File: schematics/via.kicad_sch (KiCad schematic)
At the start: 8 parts, among them J6 Port A, J7 Port B, J8 myBus, Q1 2SB817, U6 W65C22, U7 74HC238

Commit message: Fix errors in schematics
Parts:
- renumbered J6 to J4, J7 to J5, J8 to J6
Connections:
- no-connect marks 19 -> 25
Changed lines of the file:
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@@
 	)
 	(no_connect
+		(at 168.91 134.62)
+	)
+	(no_connect
 		(at 153.67 134.62)
 	)
@@
 	)
 	(no_connect
+		(at 163.83 134.62)
+	)
+	(no_connect
+		(at 173.99 134.62)
+	)
+	(no_connect
 		(at 182.88 66.04)
 	)
 	(no_connect
+		(at 166.37 134.62)
+	)
+	(no_connect
 		(at 182.88 71.12)
 	)
@@
 	)
 	(no_connect
+		(at 171.45 134.62)
+	)
+	(no_connect
 		(at 151.13 134.62)
 	)
 	(no_connect
+		(at 161.29 134.62)
+	)
+	(no_connect
 		(at 182.88 81.28)
 	)
@@
 		)
 	)
+	(label "D[0..7]"
+		(at 118.11 118.11 90)
+		(fields_autoplaced yes)
+		(effects
+			(font
+				(size 1.27 1.27)
+				(bold yes)
+			)
+			(justify left bottom)
+		)
+	)
 	(label "PA4"
 		(at 100.33 62.23 0)
@@
 		)
 	)
+	(label "PA[0..7]"
+		(at 82.55 67.31 0)
+		(fields_autoplaced yes)
+		(effects
+			(font
+				(size 1.27 1.27)
+				(bold yes)
+			)
+			(justify left bottom)
+		)
+	)
 	(label "D2"
 		(at 135.89 125.73 90)
@@
 		)
 	)
+	(label "PB[0..7]"
+		(at 82.55 105.41 0)
+		(fields_autoplaced yes)
+		(effects
+			(font
+				(size 1.27 1.27)
+				(thickness 0.254)
+				(bold yes)
+			)
+			(justify left bottom)
+		)
+	)
 	(label "A2"
 		(at 115.57 132.08 90)
@@
 		)
 	)
+	(label "A[0..3]"
+		(at 109.22 120.65 90)
+		(fields_autoplaced yes)
+		(effects
+			(font
+				(size 1.27 1.27)
+				(bold yes)
+			)
+			(justify left bottom)
+		)
+	)
 	(label "PB2"
 		(at 50.8 93.98 0)
@@
 		(dnp no)
 		(fields_autoplaced yes)
-		(property "Reference" "J7"
+		(property "Reference" "J5"
 			(at 62.865 73.66 0)
 			(effects
@@
 			(project ""
 				(path "/03a78ca6-eaff-4f05-be7b-36cd15f8b56d/61a342ed-3f86-4ceb-b427-f3e043df7103"
-					(reference "J7")
+					(reference "J5")
 					(unit 1)
 				)
@@
 		(dnp no)
 		(fields_autoplaced yes)
-		(property "Reference" "J8"
+		(property "Reference" "J6"
 			(at 125.095 149.86 0)
 			(effects
@@
 			(project ""
 				(path "/03a78ca6-eaff-4f05-be7b-36cd15f8b56d/61a342ed-3f86-4ceb-b427-f3e043df7103"
-					(reference "J8")
+					(reference "J6")
 					(unit 1)
 				)
@@
 		(dnp no)
 		(fields_autoplaced yes)
-		(property "Reference" "J6"
+		(property "Reference" "J4"
 			(at 62.865 38.1 0)
 			(effects
@@
 			(project ""
 				(path "/03a78ca6-eaff-4f05-be7b-36cd15f8b56d/61a342ed-3f86-4ceb-b427-f3e043df7103"
-					(reference "J6")
+					(reference "J4")
 					(unit 1)
 				)

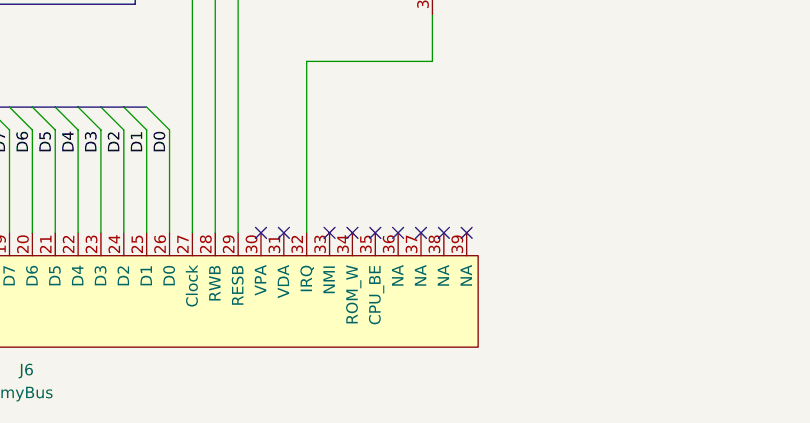
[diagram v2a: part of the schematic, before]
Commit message: Update ROM design
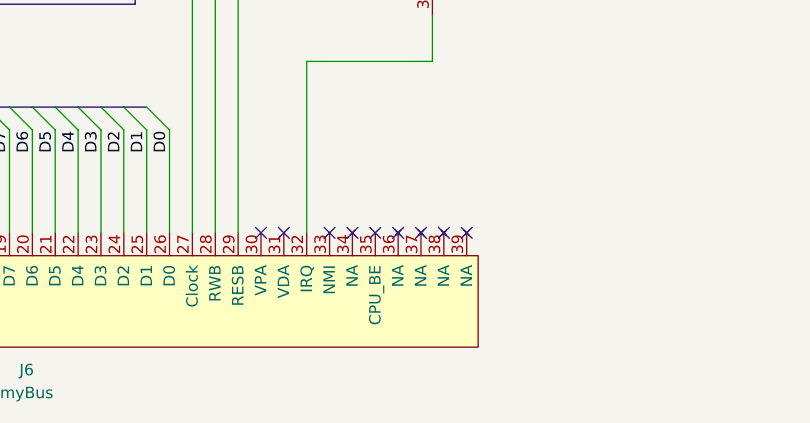
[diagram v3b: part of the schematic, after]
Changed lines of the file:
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@@
 	(label "D0"
 		(at 129.54 67.31 0)
-		(fields_autoplaced yes)
 		(effects
 			(font
@@
 	(label "CA1"
 		(at 128.27 49.53 0)
-		(fields_autoplaced yes)
 		(effects
 			(font
@@
 	(label "D1"
 		(at 138.43 125.73 90)
-		(fields_autoplaced yes)
 		(effects
 			(font
@@
 	(label "D6"
 		(at 125.73 125.73 90)
-		(fields_autoplaced yes)
 		(effects
 			(font
@@
 	(label "D[0..7]"
 		(at 118.11 118.11 90)
-		(fields_autoplaced yes)
 		(effects
 			(font
@@
 	(label "PA4"
 		(at 100.33 62.23 0)
-		(fields_autoplaced yes)
 		(effects
 			(font
@@
 	(label "PB6"
 		(at 100.33 87.63 0)
-		(fields_autoplaced yes)
 		(effects
 			(font
@@
 	(label "D6"
 		(at 129.54 82.55 0)
-		(fields_autoplaced yes)
 		(effects
 			(font
@@
 	(label "PA[0..7]"
 		(at 82.55 67.31 0)
-		(fields_autoplaced yes)
 		(effects
 			(font
@@
 	(label "D2"
 		(at 135.89 125.73 90)
-		(fields_autoplaced yes)
 		(effects
 			(font
@@
 	(label "CB2"
 		(at 105.41 95.25 180)
-		(fields_autoplaced yes)
 		(effects
 			(font
@@
 	(label "CA2"
 		(at 128.27 52.07 0)
-		(fields_autoplaced yes)
 		(effects
 			(font
@@
 	(label "PB[0..7]"
 		(at 82.55 105.41 0)
-		(fields_autoplaced yes)
 		(effects
 			(font
@@
 	(label "A2"
 		(at 115.57 132.08 90)
-		(fields_autoplaced yes)
 		(effects
 			(font
@@
 	(label "PA6"
 		(at 100.33 67.31 0)
-		(fields_autoplaced yes)
 		(effects
 			(font
@@
 	(label "A0"
 		(at 120.65 132.08 90)
-		(fields_autoplaced yes)
 		(effects
 			(font
@@
 	(label "D7"
 		(at 123.19 125.73 90)
-		(fields_autoplaced yes)
 		(effects
 			(font
@@
 	(label "PB3"
 		(at 100.33 80.01 0)
-		(fields_autoplaced yes)
 		(effects
 			(font
@@
 	(label "PA4"
 		(at 71.12 60.96 0)
-		(fields_autoplaced yes)
 		(effects
 			(font
@@
 	(label "CA1"
 		(at 54.61 50.8 180)
-		(fields_autoplaced yes)
 		(effects
 			(font
@@
 	(label "PB7"
 		(at 100.33 90.17 0)
-		(fields_autoplaced yes)
 		(effects
 			(font
@@
 	(label "D5"
 		(at 129.54 80.01 0)
-		(fields_autoplaced yes)
 		(effects
 			(font
@@
 	(label "A0"
 		(at 130.81 54.61 0)
-		(fields_autoplaced yes)
 		(effects
 			(font
@@
 	(label "PB4"
 		(at 100.33 82.55 0)
-		(fields_autoplaced yes)
 		(effects
 			(font
@@
 	(label "PA3"
 		(at 50.8 60.96 0)
-		(fields_autoplaced yes)
 		(effects
 			(font
@@
 	(label "D7"
 		(at 129.54 85.09 0)
-		(fields_autoplaced yes)
 		(effects
 			(font
@@
 	(label "PA5"
 		(at 100.33 64.77 0)
-		(fields_autoplaced yes)
 		(effects
 			(font
@@
 	(label "PB7"
 		(at 71.12 88.9 0)
-		(fields_autoplaced yes)
 		(effects
 			(font
@@
 	(label "PA7"
 		(at 100.33 69.85 0)
-		(fields_autoplaced yes)
 		(effects
 			(font
@@
 	(label "D1"
 		(at 129.54 69.85 0)
-		(fields_autoplaced yes)
 		(effects
 			(font
@@
 	(label "PB0"
 		(at 100.33 72.39 0)
-		(fields_autoplaced yes)
 		(effects
 			(font
@@
 	(label "PA1"
 		(at 50.8 55.88 0)
-		(fields_autoplaced yes)
 		(effects
 			(font
@@
 	(label "A[0..3]"
 		(at 109.22 120.65 90)
-		(fields_autoplaced yes)
 		(effects
 			(font
@@
 	(label "PB2"
 		(at 50.8 93.98 0)
-		(fields_autoplaced yes)
 		(effects
 			(font
@@
 	(label "PB1"
 		(at 50.8 91.44 0)
-		(fields_autoplaced yes)
 		(effects
 			(font
@@
 	(label "A4"
 		(at 110.49 132.08 90)
-		(fields_autoplaced yes)
 		(effects
 			(font
@@
 	(label "D4"
 		(at 130.81 125.73 90)
-		(fields_autoplaced yes)
 		(effects
 			(font
@@
 	(label "PB3"
 		(at 50.8 96.52 0)
-		(fields_autoplaced yes)
 		(effects
 			(font
@@
 	(label "PA5"
 		(at 71.12 58.42 0)
-		(fields_autoplaced yes)
 		(effects
 			(font
@@
 	(label "PA3"
 		(at 100.33 59.69 0)
-		(fields_autoplaced yes)
 		(effects
 			(font
@@
 	(label "A14"
 		(at 163.83 66.04 180)
-		(fields_autoplaced yes)
 		(effects
 			(font
@@
 	(label "A15"
 		(at 82.55 129.54 90)
-		(fields_autoplaced yes)
 		(effects
 			(font
@@
 	(label "PB4"
 		(at 71.12 96.52 0)
-		(fields_autoplaced yes)
 		(effects
 			(font
@@
 	(label "PA2"
 		(at 50.8 58.42 0)
-		(fields_autoplaced yes)
 		(effects
 			(font
@@
 	(label "PA1"
 		(at 100.33 54.61 0)
-		(fields_autoplaced yes)
 		(effects
 			(font
@@
 	(label "D2"
 		(at 129.54 72.39 0)
-		(fields_autoplaced yes)
 		(effects
 			(font
@@
 	(label "PA0"
 		(at 100.33 52.07 0)
-		(fields_autoplaced yes)
 		(effects
 			(font
@@
 	(label "PA7"
 		(at 71.12 53.34 0)
-		(fields_autoplaced yes)
 		(effects
 			(font
@@
 	(label "A4"
 		(at 163.83 68.58 180)
-		(fields_autoplaced yes)
 		(effects
 			(font
@@
 	(label "D3"
 		(at 133.35 125.73 90)
-		(fields_autoplaced yes)
 		(effects
 			(font
@@
 	(label "A1"
 		(at 118.11 132.08 90)
-		(fields_autoplaced yes)
 		(effects
 			(font
@@
 	(label "PA0"
 		(at 50.8 53.34 0)
-		(fields_autoplaced yes)
 		(effects
 			(font
@@
 	(label "PA6"
 		(at 71.12 55.88 0)
-		(fields_autoplaced yes)
 		(effects
 			(font
@@
 	(label "A3"
 		(at 130.81 62.23 0)
-		(fields_autoplaced yes)
 		(effects
 			(font
@@
 	(label "CB1"
 		(at 105.41 92.71 180)
-		(fields_autoplaced yes)
 		(effects
 			(font
@@
 	(label "PB5"
 		(at 100.33 85.09 0)
-		(fields_autoplaced yes)
 		(effects
 			(font
@@
 	(label "A2"
 		(at 130.81 59.69 0)
-		(fields_autoplaced yes)
 		(effects
 			(font
@@
 	(label "PB0"
 		(at 50.8 88.9 0)
-		(fields_autoplaced yes)
 		(effects
 			(font
@@
 	(label "CB2"
 		(at 71.12 86.36 0)
-		(fields_autoplaced yes)
 		(effects
 			(font
@@
 	(label "PA2"
 		(at 100.33 57.15 0)
-		(fields_autoplaced yes)
 		(effects
 			(font
@@
 	(label "A14"
 		(at 85.09 129.54 90)
-		(fields_autoplaced yes)
 		(effects
 			(font
@@
 	(label "PB1"
 		(at 100.33 74.93 0)
-		(fields_autoplaced yes)
 		(effects
 			(font
@@
 	(label "D0"
 		(at 140.97 125.73 90)
-		(fields_autoplaced yes)
 		(effects
 			(font
@@
 	(label "PB6"
 		(at 71.12 91.44 0)
-		(fields_autoplaced yes)
 		(effects
 			(font
@@
 	(label "A3"
 		(at 113.03 132.08 90)
-		(fields_autoplaced yes)
 		(effects
 			(font
@@
 	(label "PB2"
 		(at 100.33 77.47 0)
-		(fields_autoplaced yes)
 		(effects
 			(font
@@
 	(label "PB5"
 		(at 71.12 93.98 0)
-		(fields_autoplaced yes)
 		(effects
 			(font
@@
 	(label "D5"
 		(at 128.27 125.73 90)
-		(fields_autoplaced yes)
 		(effects
 			(font
@@
 	(label "CA2"
 		(at 71.12 50.8 0)
-		(fields_autoplaced yes)
 		(effects
 			(font
@@
 	(label "D3"
 		(at 129.54 74.93 0)
-		(fields_autoplaced yes)
 		(effects
 			(font
@@
 	(label "CB1"
 		(at 54.61 86.36 180)
-		(fields_autoplaced yes)
 		(effects
 			(font
@@
 	(label "A1"
 		(at 130.81 57.15 0)
-		(fields_autoplaced yes)
 		(effects
 			(font
@@
 	(label "A15"
 		(at 163.83 63.5 180)
-		(fields_autoplaced yes)
 		(effects
 			(font
@@
 	(label "D4"
 		(at 129.54 77.47 0)
-		(fields_autoplaced yes)
-		(effects
-			(font
+		(effects
+			(font
